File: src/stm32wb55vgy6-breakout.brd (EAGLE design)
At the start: 29 x 57.3 mm, 37 parts, among them J1 1x10, J10 PTH VERT MALE, J11 PTH VERT MALE, J2 1x10, J3 1x05 MALE VERT, J4 1x05 MALE VERT, J5 PTH VERT MALE, J6 PTH VERT MALE, J7 PTH VERT MALE, J8 PTH VERT MALE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

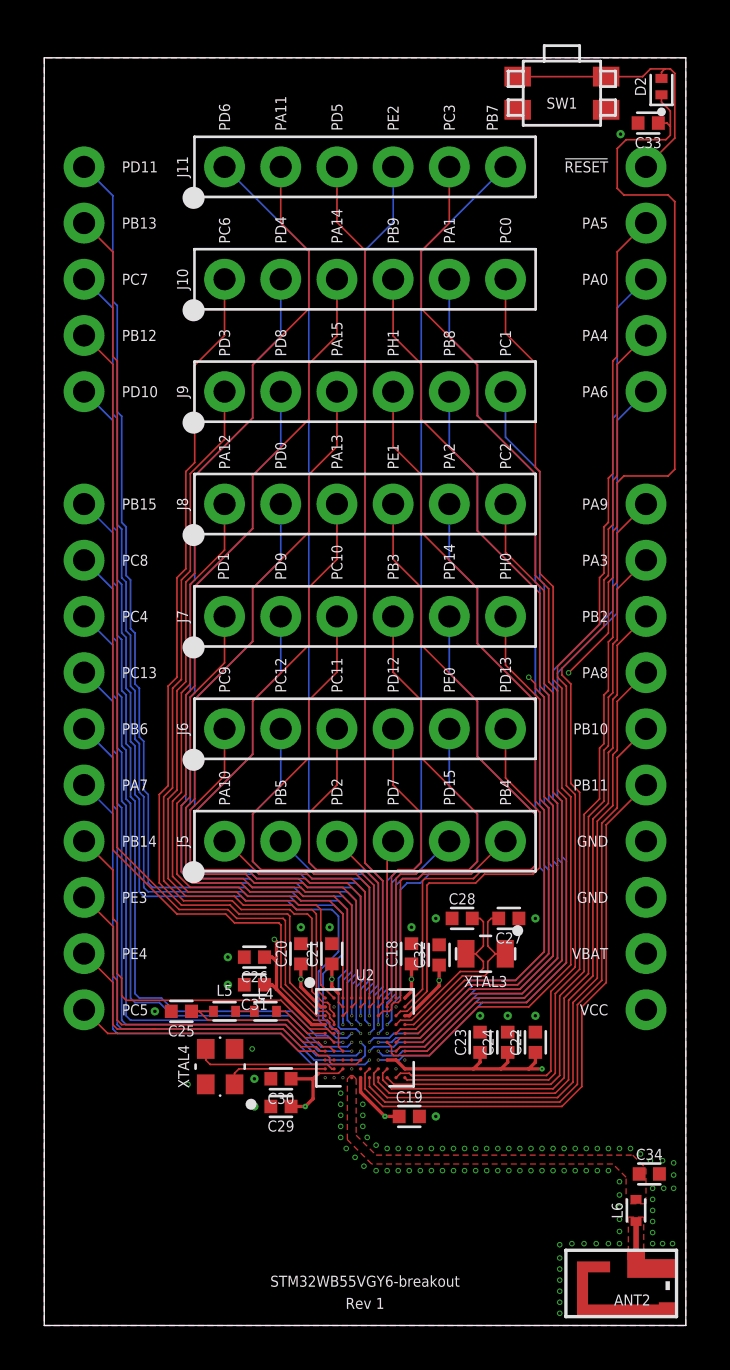
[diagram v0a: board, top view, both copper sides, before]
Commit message: [Rev 1] - Adjusted antenna microstrip width to more closely approximate a 50 ohm impedence.  Added LED power indicator to VCC.  Moved antenna circuitry to center of the board instead of the corner.
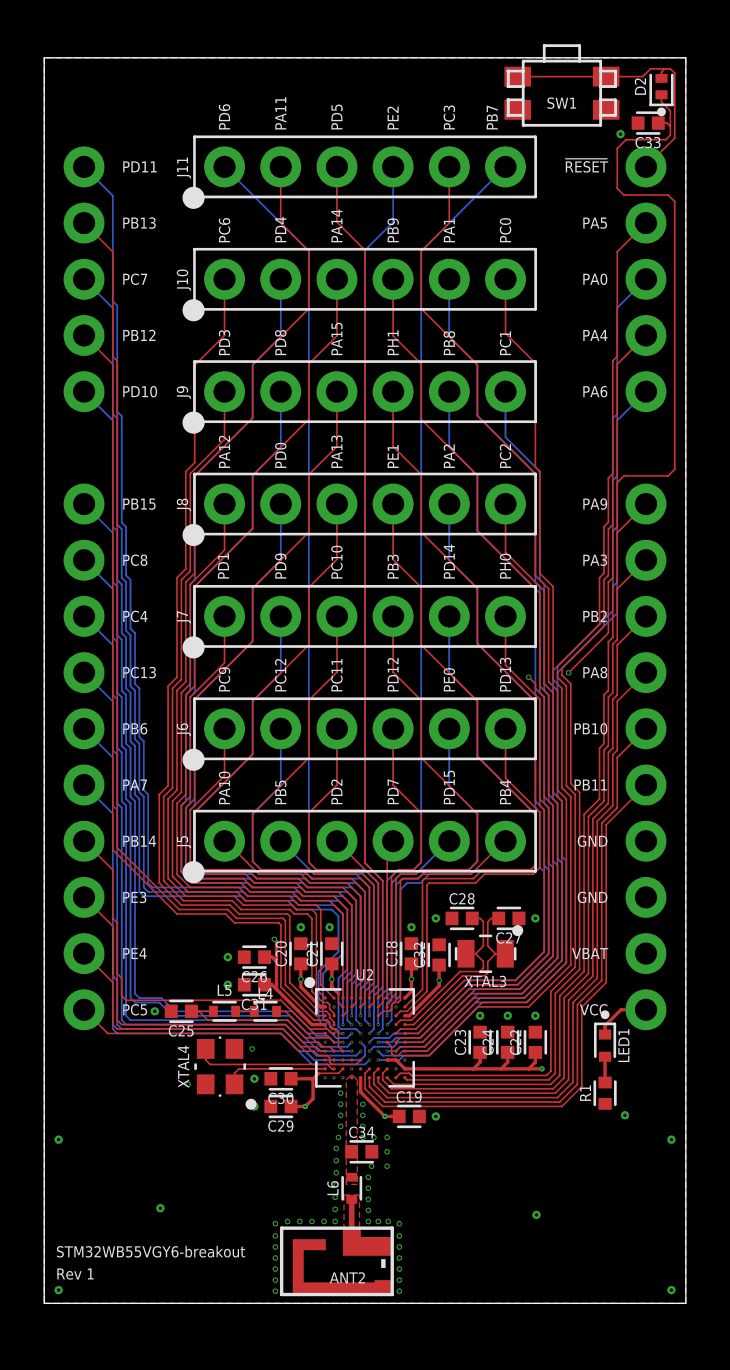
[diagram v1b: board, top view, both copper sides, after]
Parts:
- added LED1: BLUE, _leds:LEDC1005X40_LED-0402
- added R1: 10K, _resistors:RESC1005X35_SMD-0402
- moved C34 13.0 mm to (-0.15, -5.15)
- moved ANT2 12.9 mm to (1.23, -8.60)
- moved L6 12.9 mm to (-0.60, -6.80)
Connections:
- new net N$1: LED1.K, R1.2
- net GND: now also R1.1
- net VCC: now also LED1.A
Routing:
- net VCC: track 29.9 -> 32.5 mm
- net N$1: track 0.00 -> 1.17 mm
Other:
- board size 29 x 57.3 mm -> 29 x 56.3 mm
